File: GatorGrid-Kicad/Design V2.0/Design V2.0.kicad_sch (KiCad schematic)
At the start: 24 parts, among them J1 Battery-Connector, J2 Conn_01x20_Pin, J3 Conn_01x20_Pin, J4 Conn_01x20_Pin, J5 Conn_01x20_Pin, Q1 NPN, Q2 NPN, SW1 SW_SPST, U1 TP4056

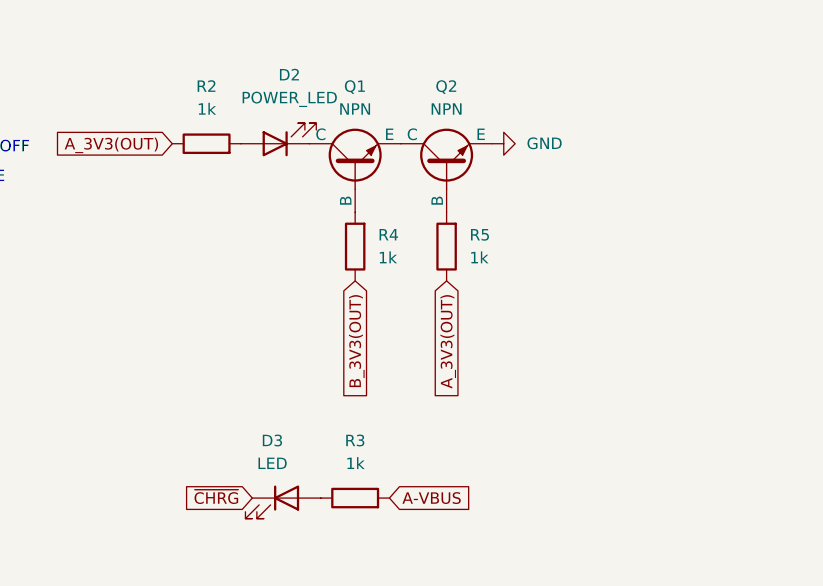
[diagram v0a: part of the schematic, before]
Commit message: edited resistor values for the AND gate circuitry
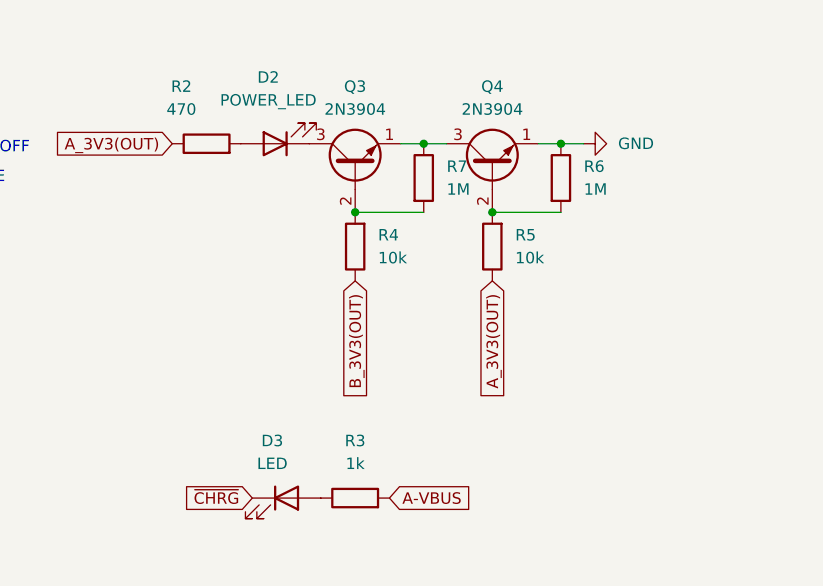
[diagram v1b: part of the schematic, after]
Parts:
- removed Q1, Q2: NPN, symbol Simulation_SPICE:NPN
- added Q3, Q4: 2N3904, Package_TO_SOT_THT:TO-92_Inline, symbol Transistor_BJT:2N3904
- added R6, R7: 1M, symbol Device:R
- R2: value 1k -> 470
- R4, R5: value 1k -> 10k
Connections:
- net GND: now also Q4.1 (E), R6.1
- net at R4.2: now also Q3.2 (B), R7.2
- net at D2.1 (K): now also Q3.3 (C)
- net at R5.2: now also Q4.2 (B), R6.2
- new net: Q3.1 (E), Q4.3 (C), R7.1
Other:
- moved on the sheet: R5

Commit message: updating KICAD
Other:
- moved on the sheet: D2, Q3, Q4, R2, R4, R5, R6, R7

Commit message: fixing KICAD
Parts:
- added D4: LED, LED_THT:LED_D5.0mm, symbol Device:LED
- added D5, D6: SS34, Diode_THT:D_DO-41_SOD81_P7.62mm_Horizontal, symbol Diode:SS34
- added R8: 1k, Resistor_THT:R_Axial_DIN0207_L6.3mm_D2.5mm_P7.62mm_Horizontal, symbol Device:R
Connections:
- net A-VBUS: now also R8.2
- net GND: now also U1.1 (TEMP)
- net VSYS: now also D5.2 (A), D6.2 (A); no longer A1.39 (VSYS), A2.39 (VSYS)
- net ~{STDBY}: now reaches U1.6 (~{STDBY})
- net ~{STDBY}: now also D4.1 (K)
- new net: A2.39 (VSYS), D6.1 (K)
- new net: A1.39 (VSYS), D5.1 (K)
- new net: D4.2 (A), R8.1
- no-connect marks 2 -> 0
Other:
- note added: "Charge Complete LED"
- note added: "Charging LED"
- note removed: "AND GATE"
- moved on the sheet: C1, C2, C3, C4, D1, F1, J1, R1, SW1, U1

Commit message: Kicad (#27)
* Version 2 complete

* adding a Version 3.0

* Added Kicad to the readme features section

* Fixing Readme's

* Fixing Readme

* Fixing Readme

* Fixing Readme

* working on it

* added an additional screw for an addition of a sensor PCB

* Finalized V3.0

* Updated Readme

* Finished V3

* Moving things

* Updated Readme

* updated Readme

* Added DHT11 library

* Working DHT11 library

---------

Co-authored-by: George Salomon <newtech20111@hotmail.com>
Co-authored-by: George Salomon <156047838+George5683@users.noreply.github.com>
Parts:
- removed D1: SS34, Diode_THT:D_DO-41_SOD81_P7.62mm_Horizontal, symbol Diode:SS34
- R6, R7: footprint (none) -> Resistor_THT:R_Axial_DIN0207_L6.3mm_D2.5mm_P7.62mm_Horizontal
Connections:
- net B_GPIO11: no longer A2.15 (GPIO11)
- net B_GPIO13: no longer J4.4 (Pin_4)
- net VSYS: now also F1.1
- net A_GPIO12 renamed UART_TX
- net UART_TX: now also A2.16 (GPIO12), J4.4 (Pin_4)
- net A_GPIO13 renamed UART_RX
- net UART_RX: now also A2.15 (GPIO11), J4.5 (Pin_5)
- removed net B_GPIO12: A2.16 (GPIO12), J4.5 (Pin_5)
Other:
- note added: "Charging Pico"
